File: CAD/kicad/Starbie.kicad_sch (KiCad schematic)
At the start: 7 parts, among them J1 Conn_01x04_Pin, J2 Conn_01x08_Pin, SW1 SW_Push, SW2 SW_Push, U1 XIAO-ESP32-C3-SMD, U2 DHT11

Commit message: see journal.md
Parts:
- added D1: D_Schottky, Diode_THT:D_DO-41_SOD81_P7.62mm_Horizontal, symbol Device:D_Schottky
- added F1: Polyfuse, Fuse:Fuse_1812_4532Metric, symbol Device:Polyfuse
- added J3: Conn_01x02, Battery:BatteryHolder_TruPower_BH-331P_3xAA, symbol Connector_Generic:Conn_01x02
- added R2: 100k, Resistor_THT:R_Axial_DIN0204_L3.6mm_D1.6mm_P7.62mm_Horizontal, symbol Device:R
- added R3: 47k, Resistor_THT:R_Axial_DIN0204_L3.6mm_D1.6mm_P7.62mm_Horizontal, symbol Device:R
- added SW3: SW_SPDT, Connector_PinHeader_2.54mm:PinHeader_1x03_P2.54mm_Vertical, symbol Switch:SW_SPDT
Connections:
- net +5V: now also D1.1 (K)
- net GND: now also J3.2 (Pin_2), R3.2
- net BAT_SENSE: now reaches U1.1 (D0)
- net BAT_SENSE: now also R2.2, R3.1
- new net: F1.1, SW3.3 (C)
- new net Battery+: J3.1 (Pin_1), SW3.2 (B)
- new net VBAT: D1.2 (A), F1.2, R2.1

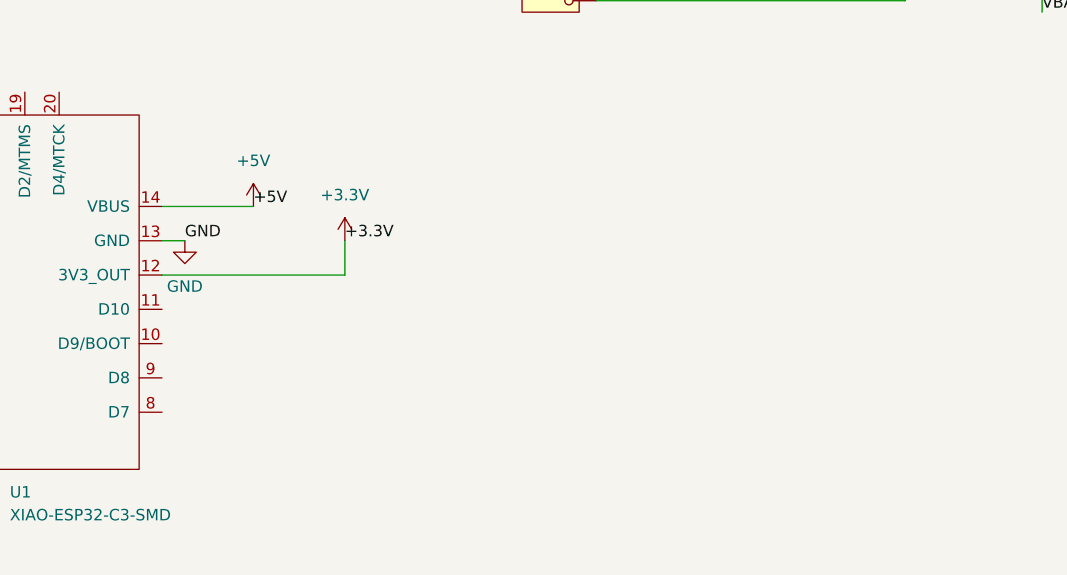
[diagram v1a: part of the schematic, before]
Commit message: Updated Gerbers and cad files with an led
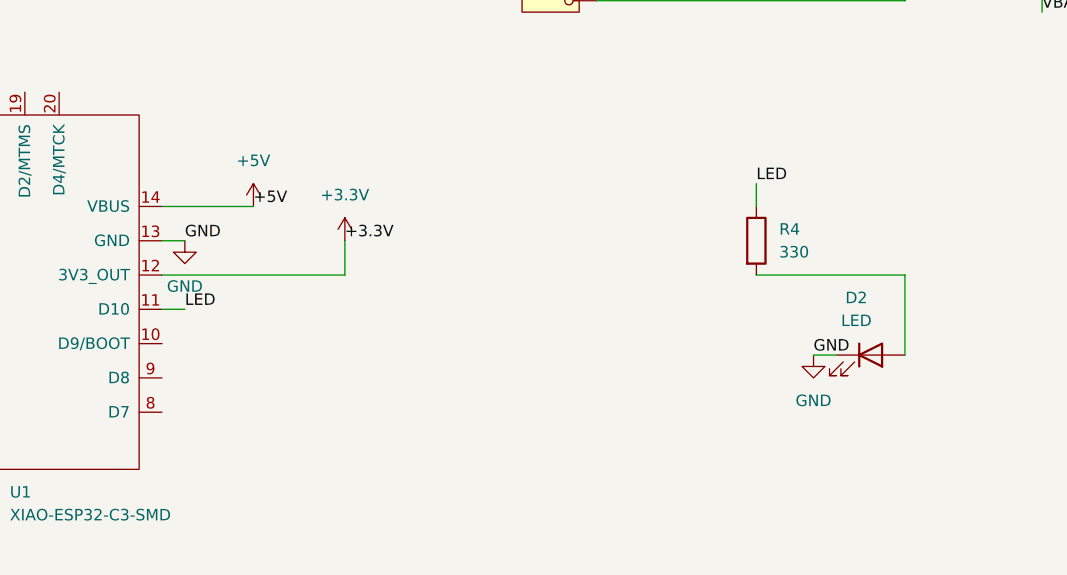
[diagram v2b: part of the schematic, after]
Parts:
- added D2: LED, LED_THT:LED_D5.0mm, symbol Device:LED
- added R4: 330, Resistor_THT:R_Axial_DIN0204_L3.6mm_D1.6mm_P7.62mm_Horizontal, symbol Device:R
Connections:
- net GND: now also D2.1 (K)
- net LED: now reaches U1.11 (D10)
- net LED: now also R4.1
- new net: D2.2 (A), R4.2
